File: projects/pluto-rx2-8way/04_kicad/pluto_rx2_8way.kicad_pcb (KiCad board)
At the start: 4 copper layers, 50 x 71 mm, 68 parts

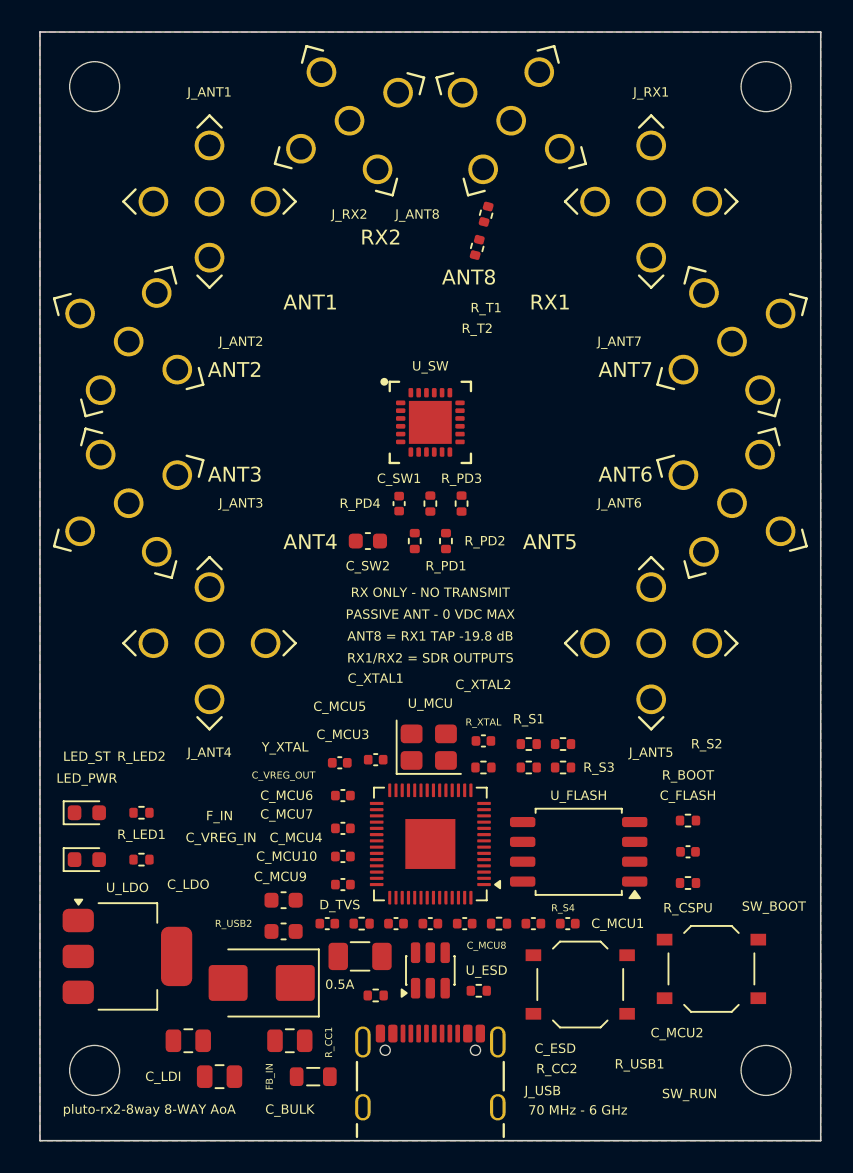
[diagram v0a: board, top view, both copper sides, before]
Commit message: pluto-rx2-8way: four of five new reds were fixable in copper, so this retires a waiver instead of adding one — and one UNREACHED budget had been FAILING at 17.194 mm with no gate able to say so
Three gate fixes landed after stage 5 closed and none of them changed a track or
a pad; they changed what is MEASURED. So every red dispositioned here was
already true and had been reported as a pass. The board's own numbers say the
gates got honest and the board did not change — except that four of the five
turned out to be FIXABLE, which is why this commit retires a waiver.

1. THE P-ADJ WAIVER IS RETIRED, AND TWO OF ITS THREE ENTRIES DISSOLVED WITHOUT
   ANY COPPER MOVING. Its closing paragraph had asked, in writing, for the
   anchor-pin metric that has now landed — a waiver arguing for a fix that
   shipped is not a judgement any more. DVDD_1V1 goes 13.167 -> 8.787 mm
   (U_MCU.23 -> C_MCU7.1) and SW_V4 goes 21.64 -> 3.057 mm (U_SW.12 -> R_PD4.1):
   the same placement, measured correctly. The 13.167 was the worst pair on a
   six-pad net and the 21.64 was a source termination ADR-0005 deliberately puts
   at the driver end.

2. ABM8 `GND <= 3 mm` WAS A REAL 0.233 mm MISS AND IS FIXED, NOT WAIVED. The old
   67.24 mm figure was the BOARD DIAGONAL. Graded against the anchor pin it read
   3.233 mm (Y_XTAL.4 -> C_XTAL1.2) and 3.140 mm (Y_XTAL.2 -> C_XTAL2.2) — the
   property the part.yaml sentence is actually about, the return path that is IN
   the oscillator loop. Both load capacitors are ROTATED 180 so their GND pad
   faces the can instead of their live pad: no coordinate moved, a 2-terminal
   0402 courtyard is symmetric so nothing else shifted, and the pair now measures
   2.457 / 2.291 mm. THE COST IS REPORTED: the live legs lengthen 1.821 -> 2.780
   (XIN) and 2.011 -> 2.915 mm (XOUT_XTAL), which against the part.yaml's OWN
   0.099 pF/mm and 3 pF stray allowance is +0.153 pF = 5.1% of the allowance,
   while the ground return shortens by 0.78 / 0.85 mm.

3. `layo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
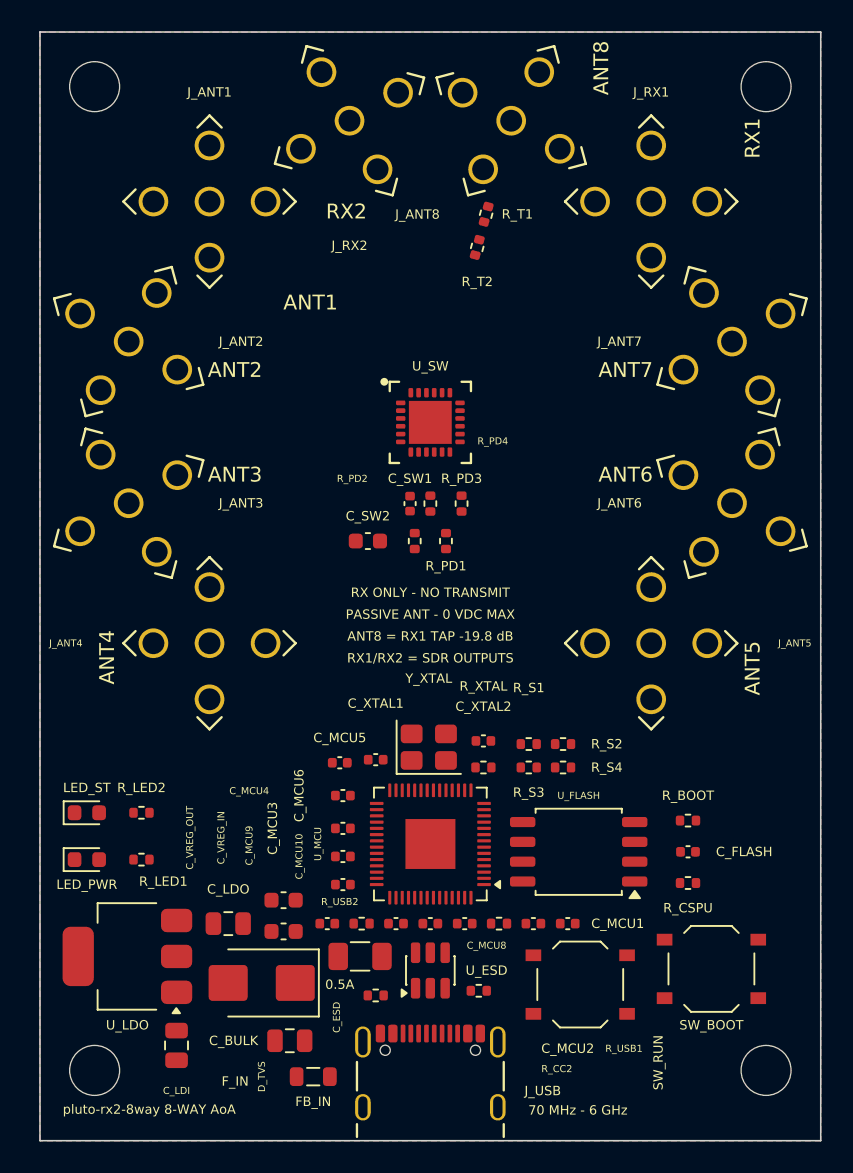
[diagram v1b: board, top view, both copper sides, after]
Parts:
- moved C_LDO 7.92 mm to (33.1, 78.1)
- moved C_LDI 3.40 mm to (29.7, 85.9), turned to -90 degrees
- moved C_SW1 0.70 mm to (44.7, 51.2)
- turned C_XTAL1 to 0 degrees
- turned C_XTAL2 to 180 degrees
- turned U_LDO to 180 degrees

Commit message: pluto-rx2-8way: the star measures 0.3236 mm — and the 49 DRC findings it costs are ONE missing constraint, not 49 problems
Board rebuilt through import -> stitch (gate: clean) -> generate_rules LAST.

THE DELIVERABLE, and for a nine-arm AoA board this number IS the deliverable:
copper_length_audit PASS, RF_RADIAL_STAR realized spread 0.3236 mm = 1.975 ps =
4.27 deg at 6 GHz against a 1.0 mm drift ceiling. 8/8 member paths measured,
and every member reports vias 0 / branch 0 / comp 1 / ends 2 — so `no_vias:
true` and `topology: chain` are VERIFIED FROM COPPER, not asserted. Arms
19.6369 (RF1/4/5) / 19.8018 (RF3/6/RFC) / 19.9604 (RF2/7) mm, 158.237 mm of arm
copper, all of it at 0.36 mm.

R-DRC 88 / 28 / 0. Parity 0. Unconnected 99 -> 28. CLASSIFIED, NEVER COUNTED:

  49 clearance  RF vs GND, 0.166..0.194 mm — the deliberate 0.14 wave budget.
                AND NOT WHERE I PREDICTED: 40 of 49 are an RF track against an
                SMA PTH GROUND POST, not against the QFN land. The launch cost
                about 9; the rest is the arm threading the jack's post square.
  21 clearance  digital, 0.175/0.1817, all VIA-vs-pad or VIA-vs-via in the MCU
                field. Not RF, not caused by this change.
  17 track_width  10 real (3V3 power taps necked to 0.1998 by KRT's
                power_tap_neckdown against a 0.4 PWR floor); 7 are a 0.2 um
                ROUNDING artifact, 0.1998 against 0.2000 — and width_floor's
                1 um tolerance would NOT lift those.
   1 starved_thermal (1 spoke of 2).

THE 49 ARE STRUCTURAL AND THE FIX IS NOT IN THIS REPO YET. A 0.36 mm arm
cannot leave PE42482A-X's land at 0.2 mm clearance — measured, it needs
<= 0.145 — so the board needs a LAUNCH-LOCAL scoped CLEARANCE rule. But
generate_rules_generic.py emits `scoped_floors` as a `track_width` constraint
ONLY; there is no clearance constraint, so this cannot be said from source
today. That is patch #4 of the 2026-07-29 escalation and it now has a MEASURED
requirement 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
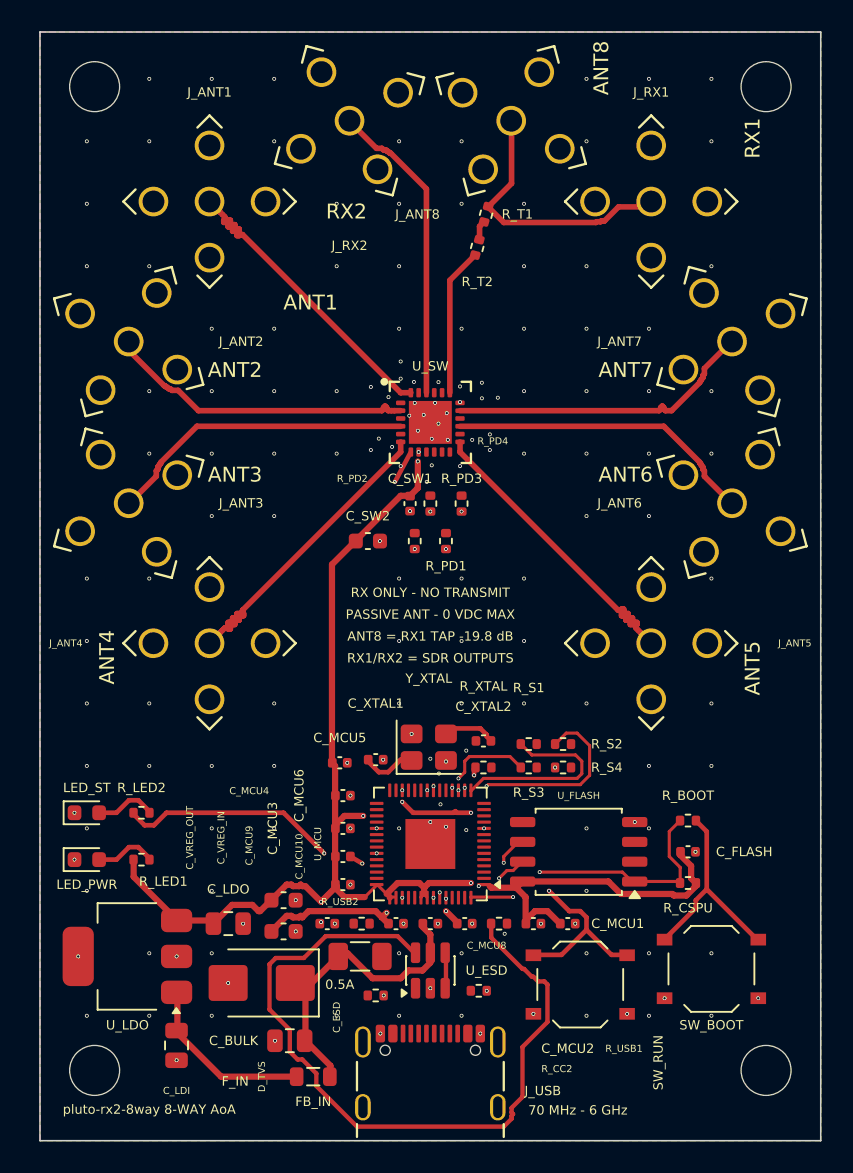
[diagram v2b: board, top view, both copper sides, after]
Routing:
- net 3V3: track 0.00 -> 95.6 mm, vias 0 -> 10
- net USB_DP: track 0.00 -> 49.0 mm
- net RUN_N: track 0.00 -> 24.6 mm, vias 0 -> 4
- net VBUS_F: track 0.00 -> 20.0 mm
- net ANT7: track 0.00 -> 20.0 mm
- net ANT2: track 0.00 -> 20.0 mm
- net RX2_OUT: track 0.00 -> 19.8 mm
- net ANT6: track 0.00 -> 19.8 mm
- net ANT3: track 0.00 -> 19.8 mm
- net ANT4: track 0.00 -> 19.6 mm
- net ANT5: track 0.00 -> 19.6 mm
- net ANT1: track 0.00 -> 19.6 mm
- net QSPI_CSN: track 0.00 -> 18.9 mm, vias 0 -> 2
- net RX1_MAIN: track 0.00 -> 17.6 mm
- net LED_STAT: track 0.00 -> 17.4 mm, vias 0 -> 2
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
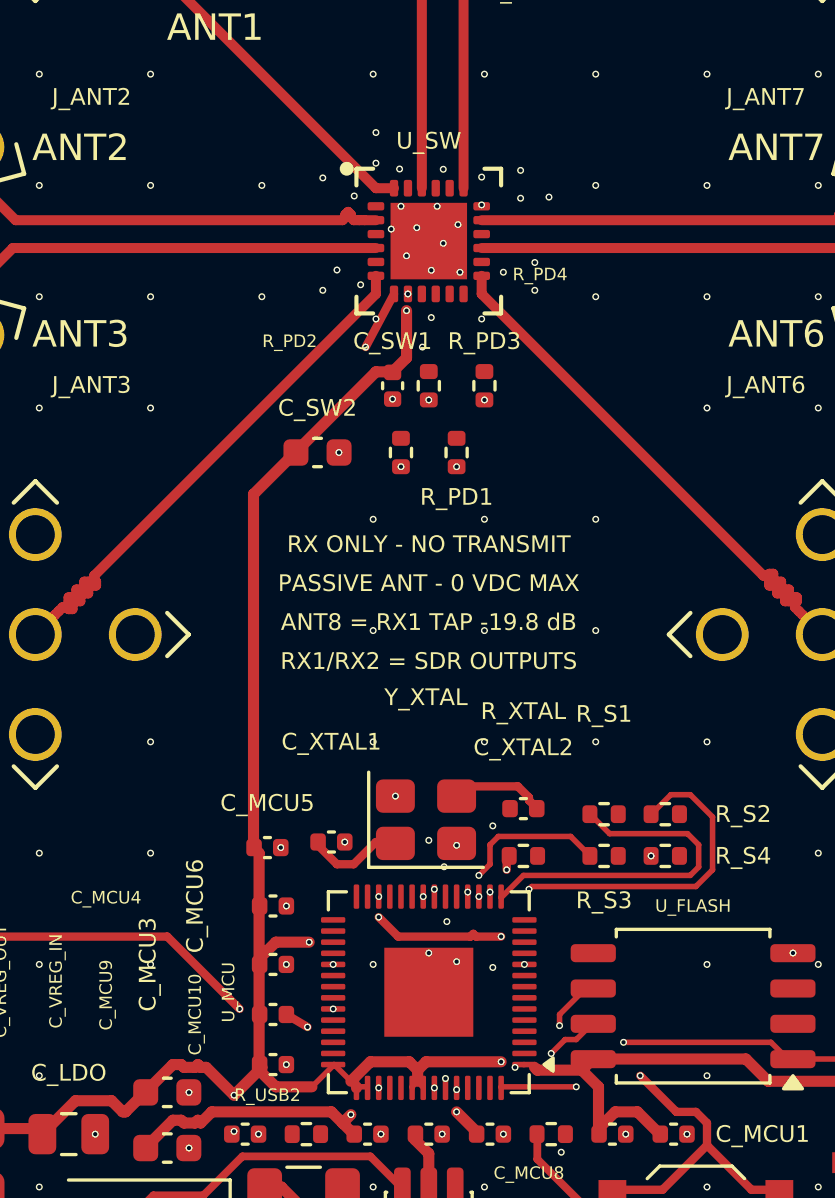
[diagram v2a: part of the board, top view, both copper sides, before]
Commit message: pad_rescue's FIRST candidate ring was already outside the bound it had to satisfy — 0.863 mm against 0.5, and no ordering of the other five could have helped
audit_board I8's single FAIL was U_SW.1's nearest GND via at 0.863 mm
against a 0.5 mm bound. The reading that mattered is not "the rescue picked
a bad site": it is that the rescue's FIRST candidate site was ALREADY
outside the bound, so the pass could never have satisfied the check that
grades it, on any board, at any angle.

MECHANISM, measured off the emitter rather than guessed.
route_and_stitch_generic._rescue_one_net computes a candidate as

    vx = px + (w2 + r) * cos(ang)
    vy = py + (h2 + r) * sin(ang)

i.e. `rings` is a distance from the pad BOUNDING-BOX EDGE, not from the pad
CENTRE — and I8's 0.5 mm is a distance from the CENTRE. U_SW.1 is a
0.60 x 0.30 land (w2 0.30, h2 0.15), so ring 0.6 puts the barrel between
0.750 mm (90 deg) and 0.900 mm (0 deg) from the centre. The 0.863 mm that
was measured is exactly ring 0.6 at the default 30 deg angle_step:
sqrt((0.9*cos30)^2 + (0.75*sin30)^2) = 0.865, on the pass's 0.01 mm
rounding grid. via_in_pad had already been tried and refused (the QFN's
0.5 mm pitch leaves no legal barrel at the land centre), so the rings were
the whole of the remaining search space.

THE FIX IS ONE PREPENDED CANDIDATE, 0.15, and the value is derived, not
picked: at 0.2 the 0 deg site lands at w2 + r = 0.500 mm — equal to the
bound with zero margin. 0.15 bounds every angle at <= 0.45 mm (0.45 at
0/180 deg, 0.30 at 90/270). It is a CANDIDATE and not a forcing: try_via
still refuses any site that breaks hole-to-copper or hole-to-hole, and the
pass falls through to 0.6 exactly as before wherever 0.15 will not fit.

MEASURED AFTER, on a rebuild_reuse.sh replay of the PROMOTED chain (never
--reroute; KRT is stochastic and the star is the deliverable):
  * audit_board  FAIL(1) -> PASS, 8 invariant groups / 16 measurements.
    U_SW.1 GND via 0.863 mm -> 0.418 mm against the 0.5 mm bo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
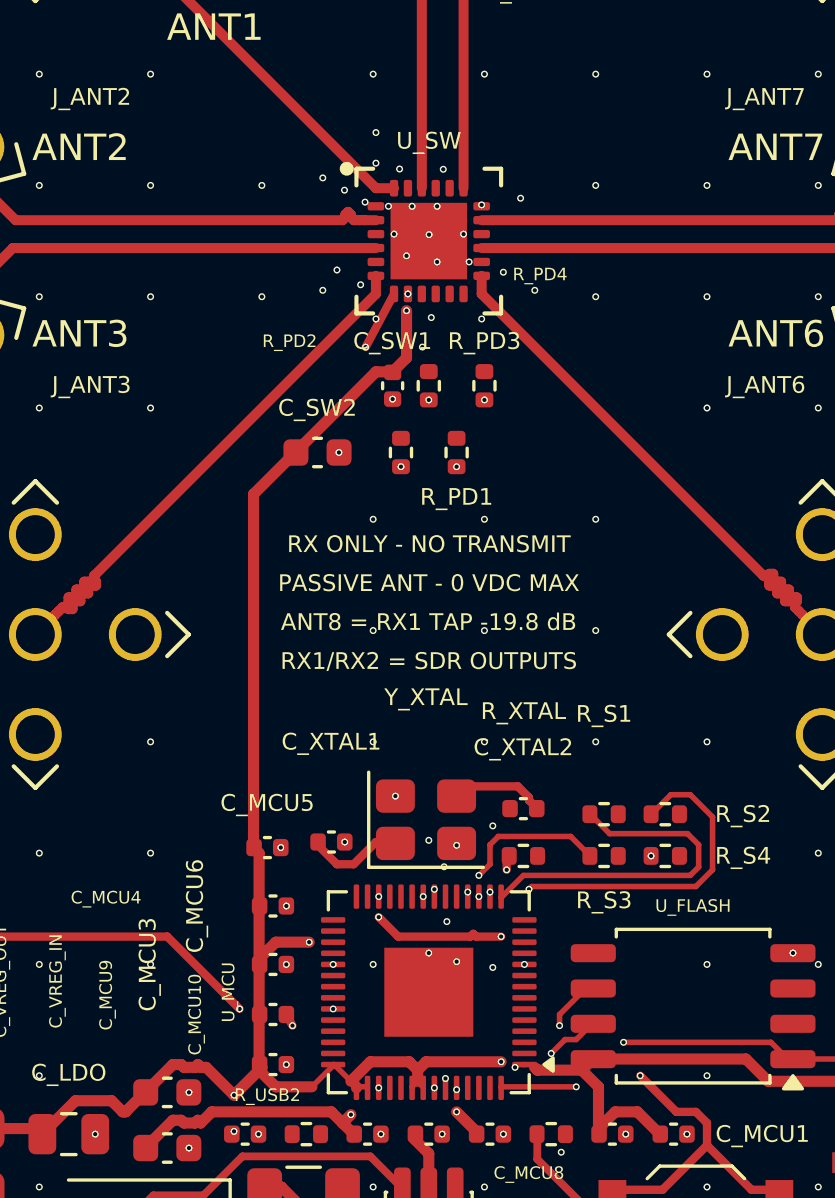
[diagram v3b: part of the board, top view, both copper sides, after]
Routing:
- net GND: track 3.05 -> 2.62 mm, vias 181 -> 178
